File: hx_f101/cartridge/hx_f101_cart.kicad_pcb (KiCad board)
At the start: 2 copper layers, 100 x 85 mm, 10 parts, among them J1 Conn_02x25_Odd_Even, J2 CONN_02x17, U1 27C128, U2 74LS245, U3 74LS133, U4 74LS32, U5 74LS04, U6 74LS07, U7 74LS07, U8 74LS00

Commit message: Add files via upload
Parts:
- added JP1: Jumper_NC_Dual, Connector_PinHeader_2.54mm:PinHeader_1x03_P2.54mm_Vertical, F.Cu at (200.5, 70.7)
- added JP2: Jumper, Connector_PinHeader_2.54mm:PinHeader_1x02_P2.54mm_Vertical, F.Cu at (217.2, 66.9)
- added JP3: Jumper, Connector_PinHeader_2.54mm:PinHeader_1x02_P2.54mm_Vertical, F.Cu at (157.5, 81.4)
- added R1: 10K, Resistor_THT:R_Axial_DIN0207_L6.3mm_D2.5mm_P10.16mm_Horizontal, F.Cu at (121.2, 92.5)
- added R2: 330R, Resistor_THT:R_Axial_DIN0207_L6.3mm_D2.5mm_P10.16mm_Horizontal, F.Cu at (216.6, 73.0)
- moved U2 53.5 mm to (126.6, 75.3)
- moved U7 29.3 mm to (157.5, 75.7)
- moved U6 26.8 mm to (179.3, 75.5)
- moved U8 23.6 mm to (202.8, 75.6), turned to 0 degrees
- moved U4 16.6 mm to (206.2, 99.4), turned to 0 degrees
- moved J2 4.10 mm to (190.4, 59.1)
- moved U5 0.76 mm to (172.7, 98.9)
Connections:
- net P18 renamed PB18
- net P20 renamed PB20
- net P22 renamed PB22
- net P24 renamed PB24
- net P26 renamed PB26
- net P28 renamed PB28
- net P30 renamed PB30
- net P32 renamed PB32
- J1 pad 13: (no net) -> _WR
- J1 pad 14: (no net) -> _RD
- J1 pad 15: (no net) -> _RESET
- J1 pad 18: (no net) -> A15
- J1 pad 25: (no net) -> A14
- J1 pad 6: (no net) -> _RFSH
- J2 pad 1: (no net) -> GND
- J2 pad 10: (no net) -> PB10
- J2 pad 12: (no net) -> PB12
- J2 pad 14: (no net) -> PB14
- J2 pad 16: (no net) -> PB16
- J2 pad 2: (no net) -> PB2
- J2 pad 34: (no net) -> PB34
- J2 pad 4: (no net) -> PB4
- J2 pad 6: (no net) -> PB6
- J2 pad 8: (no net) -> PB8
- U1 pad 20: _SLTSL -> _ROM_CE
- U1 pad 27: (no net) -> Net-(R1-Pad2)
- U2 pad 1: (no net) -> _RE
- U2 pad 19: Net-(U2-Pad19) -> _CS
- U3 pad 1: (no net) -> Net-(U3-Pad1)
- U3 pad 10: (no net) -> A8
- U3 pad 11: (no net) -> A7
- U3 pad 12: (no net) -> A6
- U3 pad 13: (no net) -> A5
- U3 pad 14: (no net) -> A4
- U3 pad 15: (no net) -> Net-(U3-Pad15)
- U3 pad 2: (no net) -> A14
- U3 pad 3: (no net) -> A13
- U3 pad 4: (no net) -> A12
- U3 pad 5: (no net) -> A11
- U3 pad 6: (no net) -> A10
- U3 pad 7: (no net) -> A9
- U3 pad 9: Net-(U2-Pad19) -> Net-(U3-Pad9)
- U4 pad 1: (no net) -> Net-(U4-Pad1)
- U4 pad 10: (no net) -> _SLTSL
- U4 pad 13: Net-(U2-Pad19) -> (no net)
- U4 pad 2: (no net) -> _SLTSL
- U4 pad 3: (no net) -> _ROM_CE
- U4 pad 4: (no net) -> _RD
- U4 pad 5: (no net) -> _SLTSL
- U4 pad 6: (no net) -> _RE
- U4 pad 8: Net-(U4-Pad8) -> _WE
- U4 pad 9: (no net) -> _WR
- U5 pad 10: Net-(U5-Pad10) -> Net-(U4-Pad1)
- U5 pad 11: (no net) -> Net-(U3-Pad9)
- U5 pad 3: (no net) -> A15
- U5 pad 4: (no net) -> Net-(U3-Pad1)
- U5 pad 5: (no net) -> A3
- U5 pad 6: (no net) -> Net-(U3-Pad15)
- U6 pad 1: (no net) -> _RE
- U6 pad 10: (no net) -> PB4
- U6 pad 11: (no net) -> _RE
- U6 pad 12: (no net) -> PB6
- U6 pad 13: (no net) -> _CS
- U6 pad 2: (no net) -> PB10
- U6 pad 3: (no net) -> _WE
- U6 pad 4: (no net) -> PB8
- U6 pad 8: (no net) -> PB2
- U6 pad 9: (no net) -> _CS
- U7 pad 1: (no net) -> Net-(JP3-Pad2)
- U7 pad 10: (no net) -> PB14
- U7 pad 11: (no net) -> A1
- U7 pad 12: (no net) -> PB16
- U7 pad 13: (no net) -> A2
- U7 pad 2: (no net) -> PB34
- U7 pad 8: (no net) -> PB12
- U7 pad 9: (no net) -> A0
- U8 pad 1: Net-(U4-Pad8) -> (no net)
- U8 pad 11: (no net) -> _CS
- U8 pad 12: (no net) -> Net-(JP1-Pad2)
- U8 pad 13: (no net) -> Net-(U4-Pad1)
- U8 pad 9: Net-(U5-Pad10) -> (no net)
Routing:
- net 5V: track 0.00 -> 254.4 mm
- net GND: track 0.00 -> 199.6 mm
- net _RE: track 0.00 -> 113.7 mm
- net _CS: track 0.00 -> 113.1 mm
- net A2: track 0.00 -> 110.2 mm, vias 0 -> 1
- net D6: track 0.00 -> 107.8 mm
- net A1: track 0.00 -> 102.6 mm, vias 0 -> 1
- net A11: track 0.00 -> 98.7 mm
- net A0: track 0.00 -> 97.7 mm, vias 0 -> 1
- net A13: track 0.00 -> 95.1 mm
- net _CS1: track 0.00 -> 94.3 mm, vias 0 -> 1
- net A8: track 0.00 -> 92.8 mm
- net A10: track 0.00 -> 92.3 mm
- net A9: track 0.00 -> 89.3 mm
- net A7: track 0.00 -> 88.7 mm
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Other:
- outline, holes or cut-outs redrawn
- net class Power added: clearance 0.4, trace_width 1.5, via_dia 2, via_drill 1

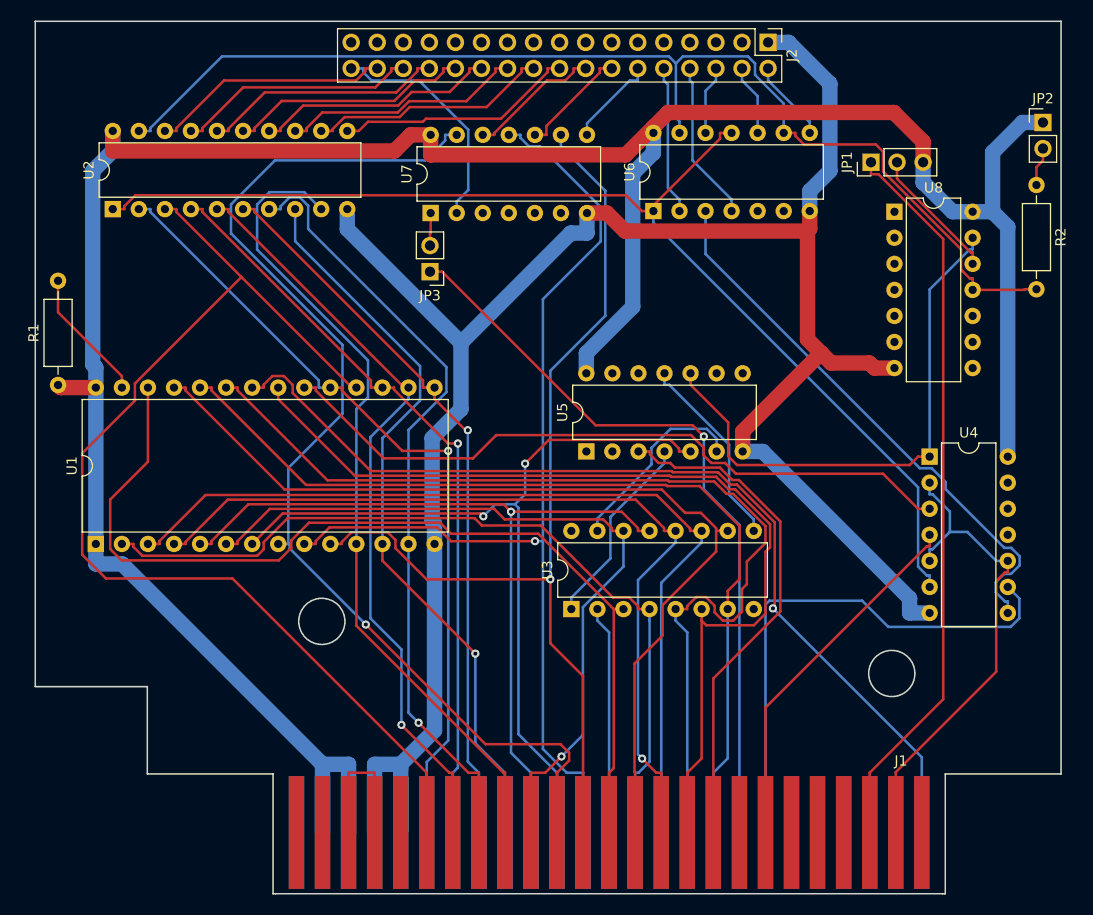
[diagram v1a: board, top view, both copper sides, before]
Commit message: update schematics and PCB. added gerber files inside zip.
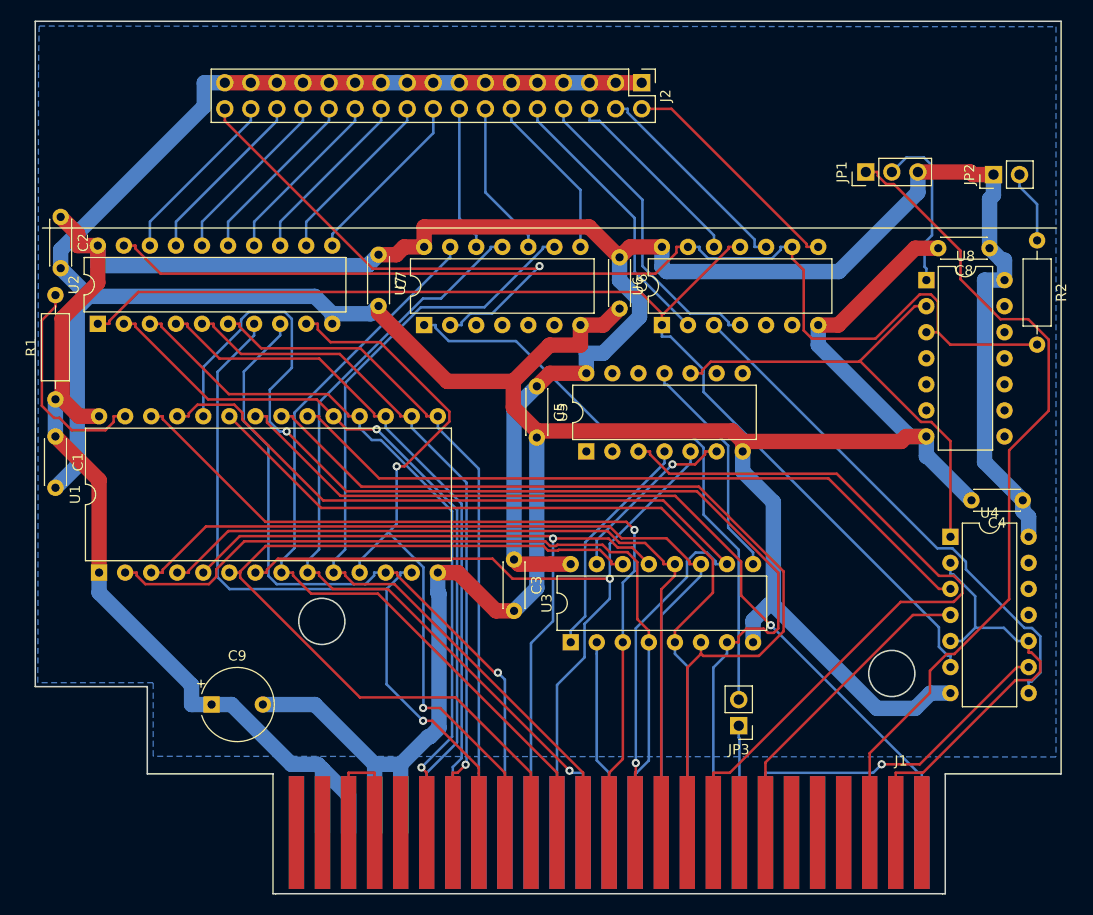
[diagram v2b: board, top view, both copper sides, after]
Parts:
- added C1: 100nF, Capacitor_THT:C_Disc_D4.3mm_W1.9mm_P5.00mm, F.Cu at (121.0, 97.5)
- added C2: 100nF, Capacitor_THT:C_Disc_D4.3mm_W1.9mm_P5.00mm, F.Cu at (121.5, 76.1)
- added C3: 100nF, Capacitor_THT:C_Disc_D4.3mm_W1.9mm_P5.00mm, F.Cu at (165.7, 109.5)
- added C4: 100nF, Capacitor_THT:C_Disc_D4.3mm_W1.9mm_P5.00mm, F.Cu at (215.3, 103.7)
- added C5: 100nF, Capacitor_THT:C_Disc_D4.3mm_W1.9mm_P5.00mm, F.Cu at (167.9, 92.6)
- added C6: 100nF, Capacitor_THT:C_Disc_D4.3mm_W1.9mm_P5.00mm, F.Cu at (176.0, 80.0)
- added C7: 100nF, Capacitor_THT:C_Disc_D4.3mm_W1.9mm_P5.00mm, F.Cu at (152.5, 79.8)
- added C8: 100nF, Capacitor_THT:C_Disc_D4.3mm_W1.9mm_P5.00mm, F.Cu at (212.0, 79.1)
- added C9: 100uF, Capacitor_THT:CP_Radial_Tantal_D7.0mm_P5.00mm, F.Cu at (136.2, 123.6)
- moved JP3 53.5 mm to (187.6, 125.7)
- moved J2 12.9 mm to (178.1, 63.0)
- moved U2 11.3 mm to (125.1, 86.5)
- moved U6 11.1 mm to (180.1, 86.6)
- moved U7 10.9 mm to (156.9, 86.6)
- moved U4 8.07 mm to (208.2, 107.3)
- moved U8 7.36 mm to (205.9, 82.2)
- moved JP2 7.01 mm to (212.4, 71.9), turned to 90 degrees
- moved R2 5.40 mm to (216.7, 78.4)
- moved U3 3.24 mm to (171.2, 117.5)
- moved U1 2.81 mm to (125.2, 110.7)
- moved R1 1.42 mm to (121.0, 93.9)
- moved JP1 1.08 mm to (200.0, 71.7)
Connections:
- J2 pad 11: (no net) -> GND
- J2 pad 13: (no net) -> GND
- J2 pad 15: (no net) -> GND
- J2 pad 17: (no net) -> GND
- J2 pad 19: (no net) -> GND
- J2 pad 21: (no net) -> GND
- J2 pad 23: (no net) -> GND
- J2 pad 25: (no net) -> GND
- J2 pad 27: (no net) -> GND
- J2 pad 29: (no net) -> GND
- J2 pad 3: (no net) -> GND
- J2 pad 31: (no net) -> GND
- J2 pad 33: (no net) -> GND
- J2 pad 5: (no net) -> GND
- J2 pad 7: (no net) -> GND
- J2 pad 9: (no net) -> GND
- U3 pad 16: (no net) -> 5V
- U3 pad 8: (no net) -> GND
- U8 pad 1: (no net) -> Net-(JP1-Pad2)
- U8 pad 11: _CS -> (no net)
- U8 pad 12: Net-(JP1-Pad2) -> (no net)
- U8 pad 13: Net-(U4-Pad1) -> (no net)
- U8 pad 2: (no net) -> Net-(U4-Pad1)
- U8 pad 3: (no net) -> _CS
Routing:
- net GND: track 199.6 -> 356.2 mm
- net _RESET: track 73.4 -> 10.4 mm, vias 1 -> 0
- net Net-(JP3-Pad2): track 3.20 -> 58.3 mm
- net D6: track 107.8 -> 70.7 mm, vias 0 -> 1
- net A2: track 110.2 -> 79.6 mm, vias 1 -> 0
- net PB34: track 22.7 -> 49.2 mm, vias 0 -> 1
- net A15: track 49.9 -> 75.3 mm
- net A9: track 89.3 -> 113.8 mm, vias 0 -> 1
- net 5V: track 254.4 -> 276.0 mm
- net A1: track 102.6 -> 82.2 mm
- net A11: track 98.7 -> 81.6 mm
- net _WR: track 52.0 -> 35.7 mm, vias 0 -> 1
- net PB8: track 15.6 -> 30.6 mm
- net PB2: track 8.02 -> 22.9 mm
- net A0: track 97.7 -> 83.4 mm, vias 1 -> 0
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- added copper zone on B.Cu, net GND
